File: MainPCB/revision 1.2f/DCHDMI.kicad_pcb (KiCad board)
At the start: 4 copper layers, 66.6 x 51.3 mm, 108 parts, among them CON1 3-1775333-2, CON2 2001-1-2-21-00-BK, CON3 CONN_01X06, U1 MCP1826S-1202E/DB, U2 MIC5219-2.5YM5-TR, U3 LP5907MFX-1.8/NOPB, U4 ADV7513, U5 664G-03LF, U6 10CL025, U7 MX25L1606EM1I-12G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

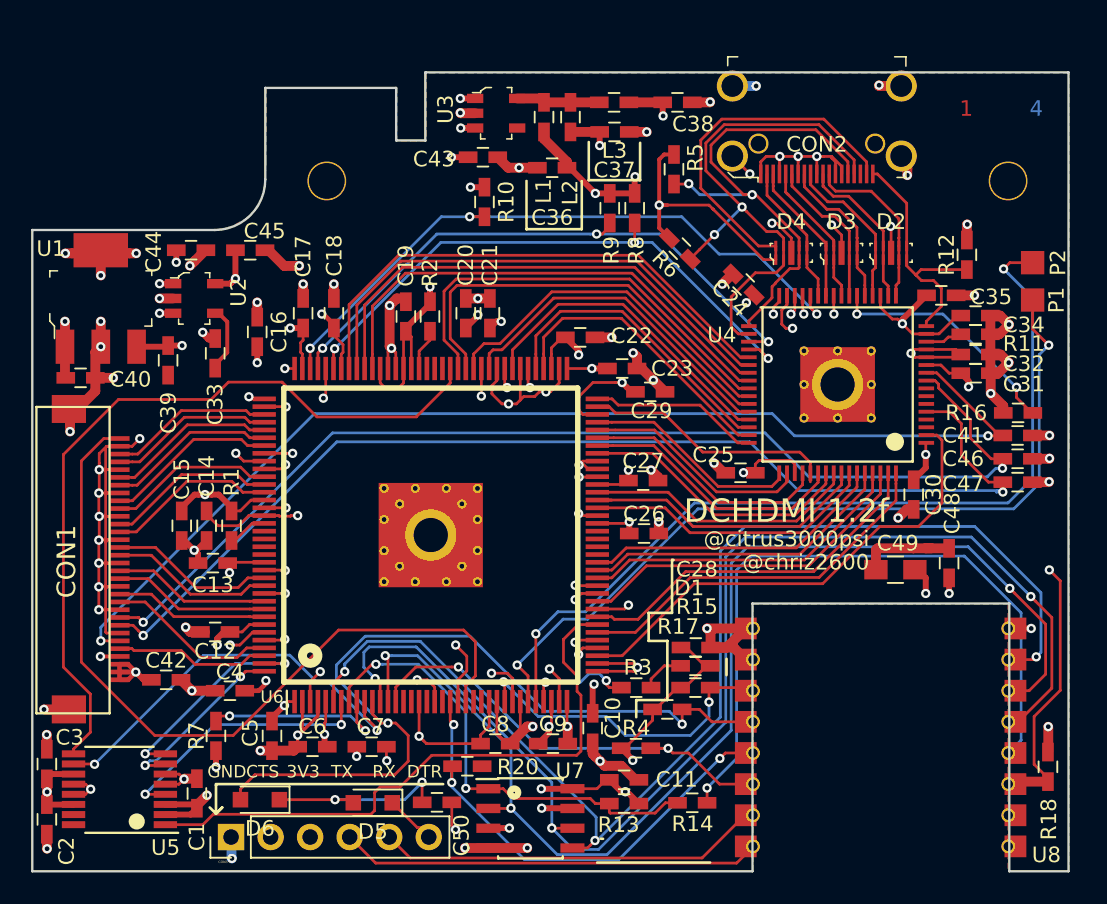
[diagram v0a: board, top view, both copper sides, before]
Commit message: 1.2 Revison
JTAG replaced with ESP header.  In Game Reset Pads added.
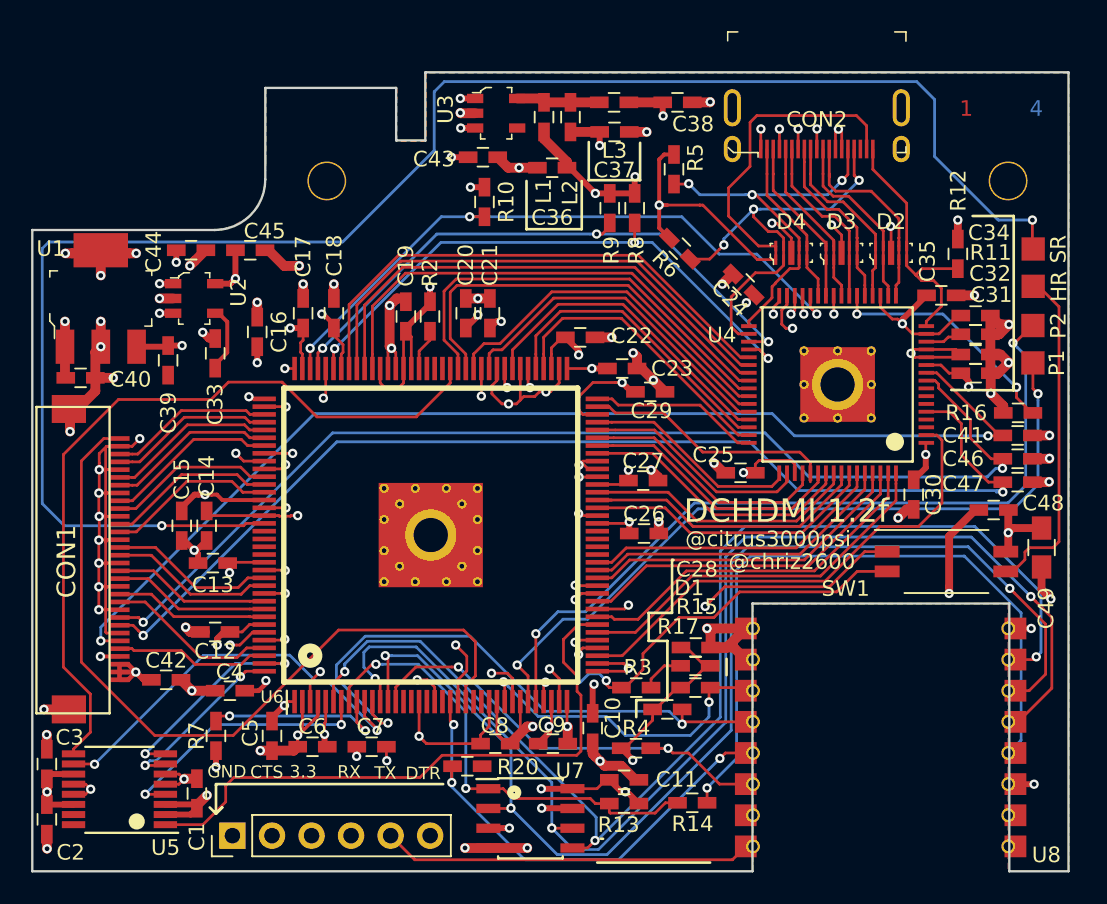
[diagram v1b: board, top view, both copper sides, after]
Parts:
- removed C50: .1u, Capacitors_SMD:C_0603_HandSoldering
- removed D5, D6: B5819WS, Diodes_SMD:D_SOD-323_HandSoldering
- removed R1, R18: 10K, Capacitors_SMD:C_0603_HandSoldering
- added CON5: CONN_01X03, pads:2_Pads_Small, F.Cu at (184.8, 85.4)
- added SW1: SW_DIP_x02, Buttons_Switches_SMD:SW_DIP_x2_W7.62mm_Slide_Copal_CHS-B, F.Cu at (180.7, 105.1)
- CON2: value 2001-1-2-21-00-BK -> DC2R019JA7R1700; footprint digikey-footprints:HDMI_Mini_Female_2001-1-2-21-00-BK -> jumper:DC2R019JA7R1700
- CON4: renamed from ?; value (none) -> CONN_01X03
- moved C49 9.50 mm to (186.8, 104.2), turned to 90 degrees
- moved C48 4.45 mm to (183.8, 101.8), turned to 0 degrees
- moved CON4 4.04 mm to (184.8, 90.3)
- moved CON2 1.60 mm to (172.4, 78.6)
- moved R12 0.58 mm to (181.5, 85.3)
- moved CON3 0.13 mm to (134.9, 122.7)
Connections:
- net Net-(R3-Pad1) renamed /HRST
- ? pad 1: /RX -> /RXD
- ? pad 1: Net-(C50-Pad2) -> +3V3
- ? pad 1: /TX -> /TXD
- CON3 pad 4: /TX -> /RXD
- CON3 pad 5: /RX -> /TXD
- U6 pad 125: Net-(R1-Pad1) -> /SRST
- U6 pad 22: GND -> Net-(U6-Pad22)
- U8 pad 15: /RX -> /RXD
- U8 pad 16: /TX -> /TXD
- U8 pad 3: Net-(C50-Pad2) -> +3V3
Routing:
- net /SRST: track 0.00 -> 109.3 mm, vias 0 -> 2
- net Net-(C50-Pad2): track 76.2 -> 0.00 mm, vias 2 -> 0
- net /RXD: track 0.00 -> 27.3 mm
- net /TX: track 27.1 -> 0.00 mm
- net /RX: track 25.1 -> 0.00 mm
- net /TXD: track 0.00 -> 23.5 mm
- net /HRST_OUT: track 0.00 -> 22.2 mm
- net /HRST: track 6.92 -> 27.7 mm
- net GND: track 237.5 -> 221.2 mm, vias 90 -> 87
- net Net-(C50-Pad1): track 12.2 -> 0.00 mm, vias 2 -> 0
- net +3V3: track 382.0 -> 392.3 mm
- net /SCL_H: track 32.3 -> 25.1 mm, vias 2 -> 3
- net /SDA_H: track 34.4 -> 27.5 mm, vias 2 -> 3
- net /PAD2: track 56.7 -> 51.0 mm
- net /ESP_SCL: track 54.0 -> 59.1 mm, vias 2 -> 3
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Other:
- board text added: "3.3"
- board text added: "HR"
- board text added: "SR"
- board text removed: "3V3"
